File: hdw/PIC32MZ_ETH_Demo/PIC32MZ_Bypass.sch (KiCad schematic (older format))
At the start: 31 parts

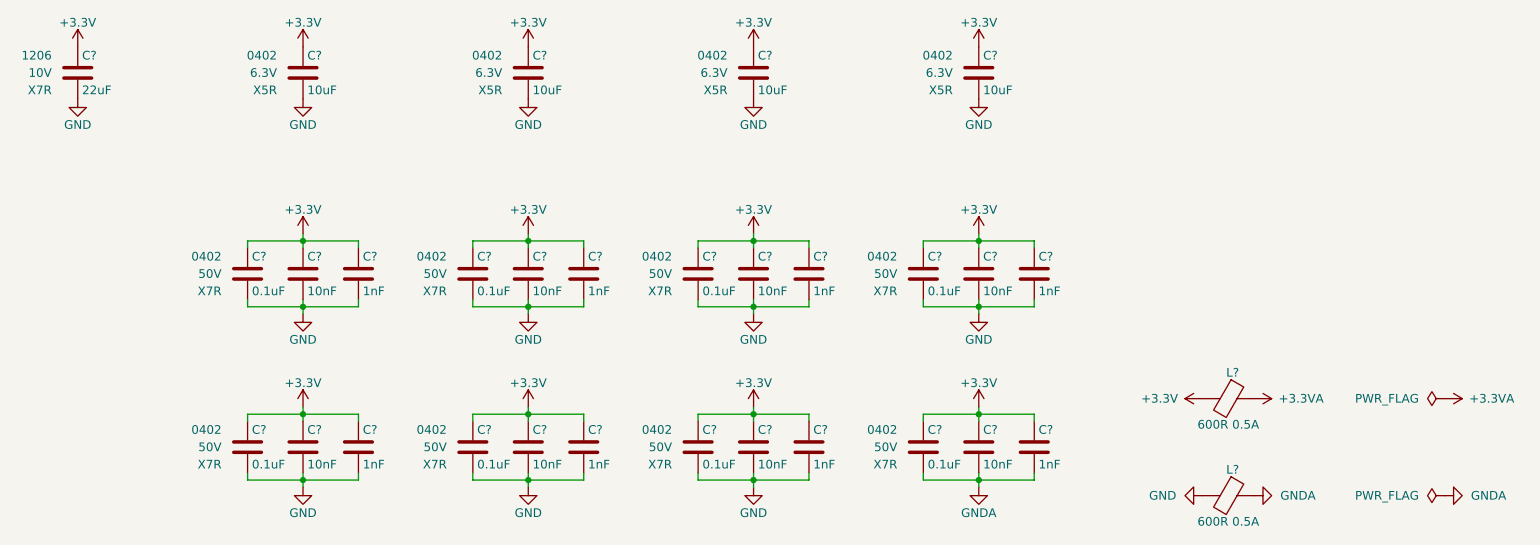
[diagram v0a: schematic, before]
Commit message: More schematic tweaks, followed PHY design guide
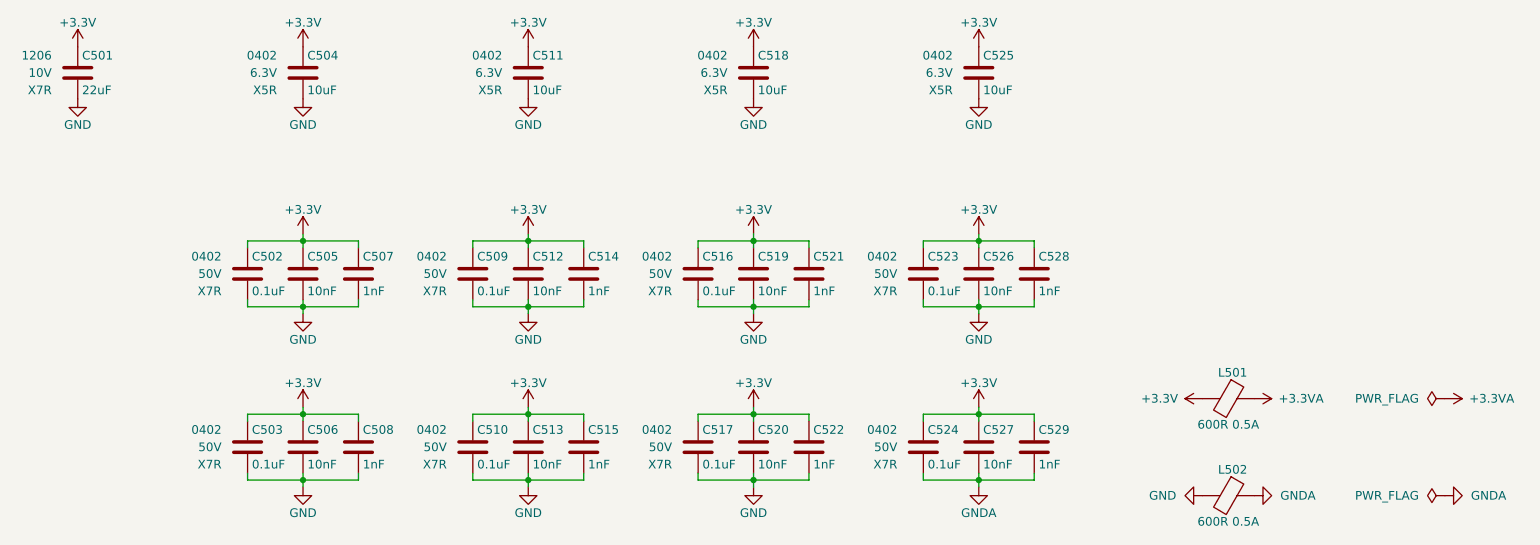
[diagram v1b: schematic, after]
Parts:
- gave numbers to parts that had none: 31

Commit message: Populated digi-key pn's
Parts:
- C502, C503, C509, C510, C516, C517, C523, C524: Digi-Key PN (none) -> 490-10701-1-ND
- C504, C511, C518, C525: Digi-Key PN (none) -> 490-13211-1-ND
- C505, C506, C512, C513, C519, C520, C526, C527: Digi-Key PN (none) -> 490-13295-1-ND
- C507, C508, C514, C515, C521, C522, C528, C529: Digi-Key PN (none) -> 399-1032-1-ND
- L501, L502: footprint Inductors_SMD:L_0603 -> Inductors_SMD:L_0402; Digi-Key PN (none) -> 490-5441-1-ND
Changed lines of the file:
@@
 F 5 "50V" H 2450 3400 50  0000 R CNN "Voltage"
 F 6 "X7R" H 2450 3300 50  0000 R CNN "Dielectric"
-F 7 "" H -1310 -3480 50  0001 C CNN "Digi-Key PN"
+F 7 "490-10701-1-ND" H -1310 -3480 50  0001 C CNN "Digi-Key PN"
 	1    2600 3400
 	1    0    0    -1
@@
 F 5 "50V" H 3090 3400 50  0001 R CNN "Voltage"
 F 6 "X7R" H 3090 3300 50  0001 R CNN "Dielectric"
-F 7 "" H -1310 -3480 50  0001 C CNN "Digi-Key PN"
+F 7 "399-1032-1-ND" H -1310 -3480 50  0001 C CNN "Digi-Key PN"
 	1    3240 3400
 	1    0    0    -1
@@
 F 5 "50V" H 2770 3400 50  0001 R CNN "Voltage"
 F 6 "X7R" H 2770 3300 50  0001 R CNN "Dielectric"
-F 7 "" H -1310 -3480 50  0001 C CNN "Digi-Key PN"
+F 7 "490-13295-1-ND" H -1310 -3480 50  0001 C CNN "Digi-Key PN"
 	1    2920 3400
 	1    0    0    -1
@@
 F 5 "50V" H 3750 3400 50  0000 R CNN "Voltage"
 F 6 "X7R" H 3750 3300 50  0000 R CNN "Dielectric"
-F 7 "" H -10 -3480 50  0001 C CNN "Digi-Key PN"
+F 7 "490-10701-1-ND" H -10 -3480 50  0001 C CNN "Digi-Key PN"
 	1    3900 3400
 	1    0    0    -1
@@
 F 5 "50V" H 4390 3400 50  0001 R CNN "Voltage"
 F 6 "X7R" H 4390 3300 50  0001 R CNN "Dielectric"
-F 7 "" H -10 -3480 50  0001 C CNN "Digi-Key PN"
+F 7 "399-1032-1-ND" H -10 -3480 50  0001 C CNN "Digi-Key PN"
 	1    4540 3400
 	1    0    0    -1
@@
 F 5 "50V" H 4070 3400 50  0001 R CNN "Voltage"
 F 6 "X7R" H 4070 3300 50  0001 R CNN "Dielectric"
-F 7 "" H -10 -3480 50  0001 C CNN "Digi-Key PN"
+F 7 "490-13295-1-ND" H -10 -3480 50  0001 C CNN "Digi-Key PN"
 	1    4220 3400
 	1    0    0    -1
@@
 F 5 "50V" H 5050 3400 50  0000 R CNN "Voltage"
 F 6 "X7R" H 5050 3300 50  0000 R CNN "Dielectric"
-F 7 "" H 1290 -3480 50  0001 C CNN "Digi-Key PN"
+F 7 "490-10701-1-ND" H 1290 -3480 50  0001 C CNN "Digi-Key PN"
 	1    5200 3400
 	1    0    0    -1
@@
 F 5 "50V" H 5690 3400 50  0001 R CNN "Voltage"
 F 6 "X7R" H 5690 3300 50  0001 R CNN "Dielectric"
-F 7 "" H 1290 -3480 50  0001 C CNN "Digi-Key PN"
+F 7 "399-1032-1-ND" H 1290 -3480 50  0001 C CNN "Digi-Key PN"
 	1    5840 3400
 	1    0    0    -1
@@
 F 5 "50V" H 5370 3400 50  0001 R CNN "Voltage"
 F 6 "X7R" H 5370 3300 50  0001 R CNN "Dielectric"
-F 7 "" H 1290 -3480 50  0001 C CNN "Digi-Key PN"
+F 7 "490-13295-1-ND" H 1290 -3480 50  0001 C CNN "Digi-Key PN"
 	1    5520 3400
 	1    0    0    -1
@@
 F 5 "50V" H 6350 3400 50  0000 R CNN "Voltage"
 F 6 "X7R" H 6350 3300 50  0000 R CNN "Dielectric"
-F 7 "" H 2590 -3480 50  0001 C CNN "Digi-Key PN"
+F 7 "490-10701-1-ND" H 2590 -3480 50  0001 C CNN "Digi-Key PN"
 	1    6500 3400
 	1    0    0    -1
@@
 F 5 "50V" H 6990 3400 50  0001 R CNN "Voltage"
 F 6 "X7R" H 6990 3300 50  0001 R CNN "Dielectric"
-F 7 "" H 2590 -3480 50  0001 C CNN "Digi-Key PN"
+F 7 "399-1032-1-ND" H 2590 -3480 50  0001 C CNN "Digi-Key PN"
 	1    7140 3400
 	1    0    0    -1
@@
 F 5 "50V" H 6670 3400 50  0001 R CNN "Voltage"
 F 6 "X7R" H 6670 3300 50  0001 R CNN "Dielectric"
-F 7 "" H 2590 -3480 50  0001 C CNN "Digi-Key PN"
+F 7 "490-13295-1-ND" H 2590 -3480 50  0001 C CNN "Digi-Key PN"
 	1    6820 3400
 	1    0    0    -1
@@
 F 5 "50V" H 2450 4400 50  0000 R CNN "Voltage"
 F 6 "X7R" H 2450 4300 50  0000 R CNN "Dielectric"
-F 7 "" H -1310 -2480 50  0001 C CNN "Digi-Key PN"
+F 7 "490-10701-1-ND" H -1310 -2480 50  0001 C CNN "Digi-Key PN"
 	1    2600 4400
 	1    0    0    -1
@@
 F 5 "50V" H 3090 4400 50  0001 R CNN "Voltage"
 F 6 "X7R" H 3090 4300 50  0001 R CNN "Dielectric"
-F 7 "" H -1310 -2480 50  0001 C CNN "Digi-Key PN"
+F 7 "399-1032-1-ND" H -1310 -2480 50  0001 C CNN "Digi-Key PN"
 	1    3240 4400
 	1    0    0    -1
@@
 F 5 "50V" H 2770 4400 50  0001 R CNN "Voltage"
 F 6 "X7R" H 2770 4300 50  0001 R CNN "Dielectric"
-F 7 "" H -1310 -2480 50  0001 C CNN "Digi-Key PN"
+F 7 "490-13295-1-ND" H -1310 -2480 50  0001 C CNN "Digi-Key PN"
 	1    2920 4400
 	1    0    0    -1
@@
 F 5 "50V" H 3750 4400 50  0000 R CNN "Voltage"
 F 6 "X7R" H 3750 4300 50  0000 R CNN "Dielectric"
-F 7 "" H -10 -2480 50  0001 C CNN "Digi-Key PN"
+F 7 "490-10701-1-ND" H -10 -2480 50  0001 C CNN "Digi-Key PN"
 	1    3900 4400
 	1    0    0    -1
@@
 F 5 "50V" H 4390 4400 50  0001 R CNN "Voltage"
 F 6 "X7R" H 4390 4300 50  0001 R CNN "Dielectric"
-F 7 "" H -10 -2480 50  0001 C CNN "Digi-Key PN"
+F 7 "399-1032-1-ND" H -10 -2480 50  0001 C CNN "Digi-Key PN"
 	1    4540 4400
 	1    0    0    -1
@@
 F 5 "50V" H 4070 4400 50  0001 R CNN "Voltage"
 F 6 "X7R" H 4070 4300 50  0001 R CNN "Dielectric"
-F 7 "" H -10 -2480 50  0001 C CNN "Digi-Key PN"
+F 7 "490-13295-1-ND" H -10 -2480 50  0001 C CNN "Digi-Key PN"
 	1    4220 4400
 	1    0    0    -1
@@
 F 5 "50V" H 5050 4400 50  0000 R CNN "Voltage"
 F 6 "X7R" H 5050 4300 50  0000 R CNN "Dielectric"
-F 7 "" H 1290 -2480 50  0001 C CNN "Digi-Key PN"
+F 7 "490-10701-1-ND" H 1290 -2480 50  0001 C CNN "Digi-Key PN"
 	1    5200 4400
 	1    0    0    -1
@@
 F 5 "50V" H 5690 4400 50  0001 R CNN "Voltage"
 F 6 "X7R" H 5690 4300 50  0001 R CNN "Dielectric"
-F 7 "" H 1290 -2480 50  0001 C CNN "Digi-Key PN"
+F 7 "399-1032-1-ND" H 1290 -2480 50  0001 C CNN "Digi-Key PN"
 	1    5840 4400
 	1    0    0    -1
@@
 F 5 "50V" H 5370 4400 50  0001 R CNN "Voltage"
 F 6 "X7R" H 5370 4300 50  0001 R CNN "Dielectric"
-F 7 "" H 1290 -2480 50  0001 C CNN "Digi-Key PN"
+F 7 "490-13295-1-ND" H 1290 -2480 50  0001 C CNN "Digi-Key PN"
 	1    5520 4400
 	1    0    0    -1
@@
 F 5 "50V" H 6670 4400 50  0001 R CNN "Voltage"
 F 6 "X7R" H 6670 4300 50  0001 R CNN "Dielectric"
-F 7 "" H 2590 -2480 50  0001 C CNN "Digi-Key PN"
+F 7 "490-13295-1-ND" H 2590 -2480 50  0001 C CNN "Digi-Key PN"
 	1    6820 4400
 	1    0    0    -1
@@
 F 5 "50V" H 6990 4400 50  0001 R CNN "Voltage"
 F 6 "X7R" H 6990 4300 50  0001 R CNN "Dielectric"
-F 7 "" H 2590 -2480 50  0001 C CNN "Digi-Key PN"
+F 7 "399-1032-1-ND" H 2590 -2480 50  0001 C CNN "Digi-Key PN"
 	1    7140 4400
 	1    0    0    -1
@@
 F 5 "50V" H 6350 4400 50  0000 R CNN "Voltage"
 F 6 "X7R" H 6350 4300 50  0000 R CNN "Dielectric"
-F 7 "" H 2590 -2480 50  0001 C CNN "Digi-Key PN"
+F 7 "490-10701-1-ND" H 2590 -2480 50  0001 C CNN "Digi-Key PN"
 	1    6500 4400
 	1    0    0    -1
@@
 F 0 "L501" V 8110 4145 50  0000 C CNN
 F 1 "600R 0.5A" V 8410 4120 50  0000 C CNN
-F 2 "Inductors_SMD:L_0603" V 8190 4120 50  0001 C CNN
+F 2 "Inductors_SMD:L_0402" V 8190 4120 50  0001 C CNN
 F 3 "~" H 8260 4120 50  0001 C CNN
-F 4 "" H -1270 360 50  0001 C CNN "Digi-Key PN"
+F 4 "490-5441-1-ND" H -1270 360 50  0001 C CNN "Digi-Key PN"
 	1    8260 4120
 	0    1    1    0
@@
 F 0 "L502" V 8110 4705 50  0000 C CNN
 F 1 "600R 0.5A" V 8410 4680 50  0000 C CNN
-F 2 "Inductors_SMD:L_0603" V 8190 4680 50  0001 C CNN
+F 2 "Inductors_SMD:L_0402" V 8190 4680 50  0001 C CNN
 F 3 "~" H 8260 4680 50  0001 C CNN
-F 4 "" H -1270 920 50  0001 C CNN "Digi-Key PN"
+F 4 "490-5441-1-ND" H -1270 920 50  0001 C CNN "Digi-Key PN"
 	1    8260 4680
 	0    1    1    0
@@
 F 5 "6.3V" H 2770 2240 50  0000 R CNN "Voltage"
 F 6 "X5R" H 2770 2140 50  0000 R CNN "Dielectric"
-F 7 "" H 2920 2240 50  0001 C CNN "Digi-Key PN"
+F 7 "490-13211-1-ND" H 2920 2240 50  0001 C CNN "Digi-Key PN"
 	1    2920 2240
 	1    0    0    -1
@@
 F 5 "6.3V" H 4070 2240 50  0000 R CNN "Voltage"
 F 6 "X5R" H 4070 2140 50  0000 R CNN "Dielectric"
-F 7 "" H 4220 2240 50  0001 C CNN "Digi-Key PN"
+F 7 "490-13211-1-ND" H 4220 2240 50  0001 C CNN "Digi-Key PN"
 	1    4220 2240
 	1    0    0    -1
@@
 F 5 "6.3V" H 5370 2240 50  0000 R CNN "Voltage"
 F 6 "X5R" H 5370 2140 50  0000 R CNN "Dielectric"
-F 7 "" H 5520 2240 50  0001 C CNN "Digi-Key PN"
+F 7 "490-13211-1-ND" H 5520 2240 50  0001 C CNN "Digi-Key PN"
 	1    5520 2240
 	1    0    0    -1
@@
 F 5 "6.3V" H 6670 2240 50  0000 R CNN "Voltage"
 F 6 "X5R" H 6670 2140 50  0000 R CNN "Dielectric"
-F 7 "" H 6820 2240 50  0001 C CNN "Digi-Key PN"
+F 7 "490-13211-1-ND" H 6820 2240 50  0001 C CNN "Digi-Key PN"
 	1    6820 2240
 	1    0    0    -1

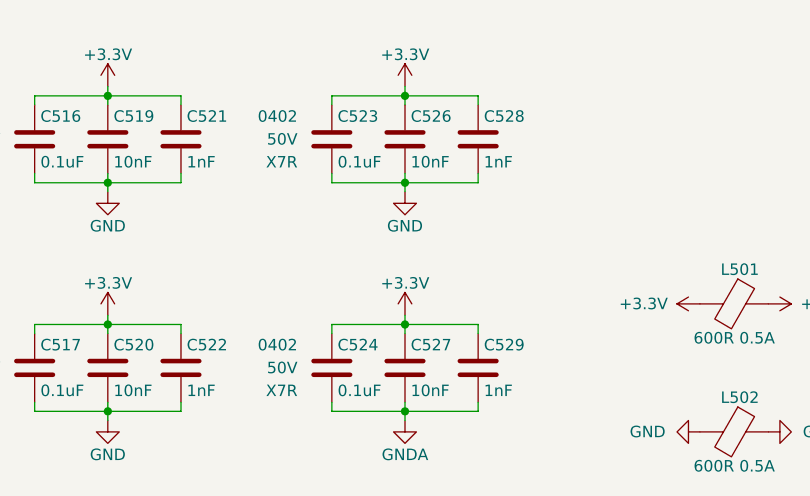
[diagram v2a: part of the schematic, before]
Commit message: Started arranging parts on PCB
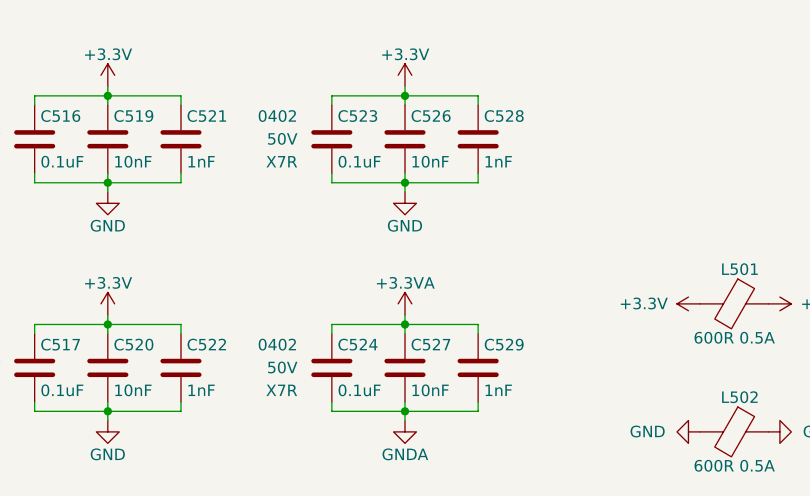
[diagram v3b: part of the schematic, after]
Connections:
- net +3.3VA: now also C524.1, C527.1, C529.1
- net +3V3: no longer C524.1, C527.1, C529.1
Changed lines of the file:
@@
-$EndComp
-$Comp
-L power:+3.3V #PWR0525
-U 1 1 5E6E5A5E
-P 6820 4170
-F 0 "#PWR0525" H 6820 4020 50  0001 C CNN
-F 1 "+3.3V" H 6820 4310 50  0000 C CNN
-F 2 "" H 6820 4170 50  0001 C CNN
-F 3 "" H 6820 4170 50  0001 C CNN
-	1    6820 4170
-	1    0    0    -1
 $EndComp
 $Comp
@@
 	0    -1   -1   0
 $EndComp
+$Comp
+L power:+3.3VA #PWR0101
+U 1 1 5E8A98BF
+P 6820 4170
+F 0 "#PWR0101" H 6820 4020 50  0001 C CNN
+F 1 "+3.3VA" H 6820 4310 50  0000 C CNN
+F 2 "" H 6820 4170 50  0001 C CNN
+F 3 "" H 6820 4170 50  0001 C CNN
+	1    6820 4170
+	1    0    0    -1
+$EndComp
 $EndSCHEMATC
